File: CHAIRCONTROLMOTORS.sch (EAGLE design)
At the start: 39 parts, among them IC2 TCAN332DR, IC3 ATMEGA328P, IC4 MCP2515

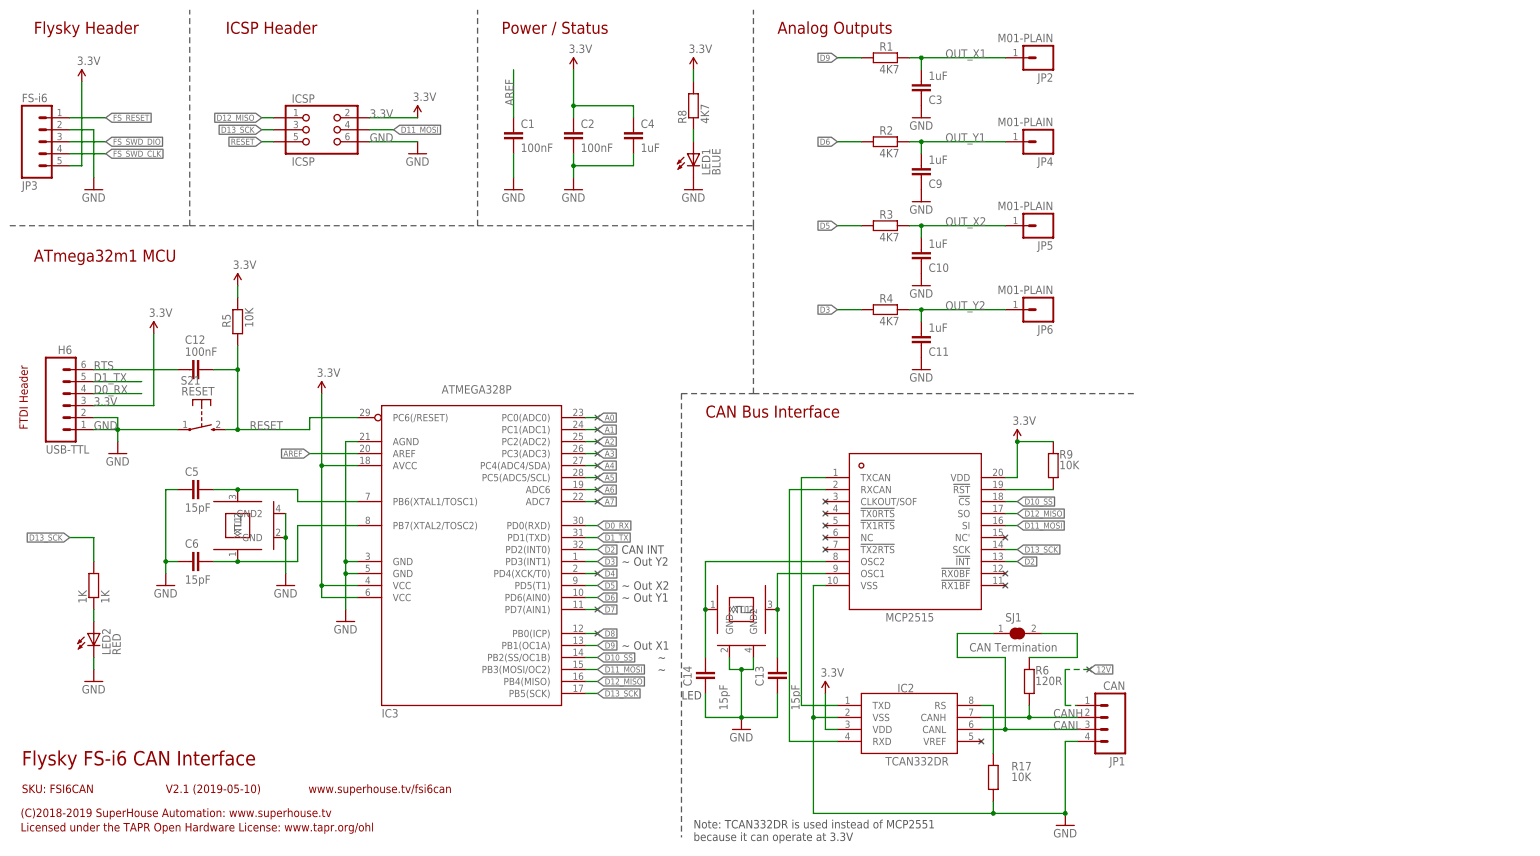
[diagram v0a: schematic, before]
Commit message: Added XTxx external connections
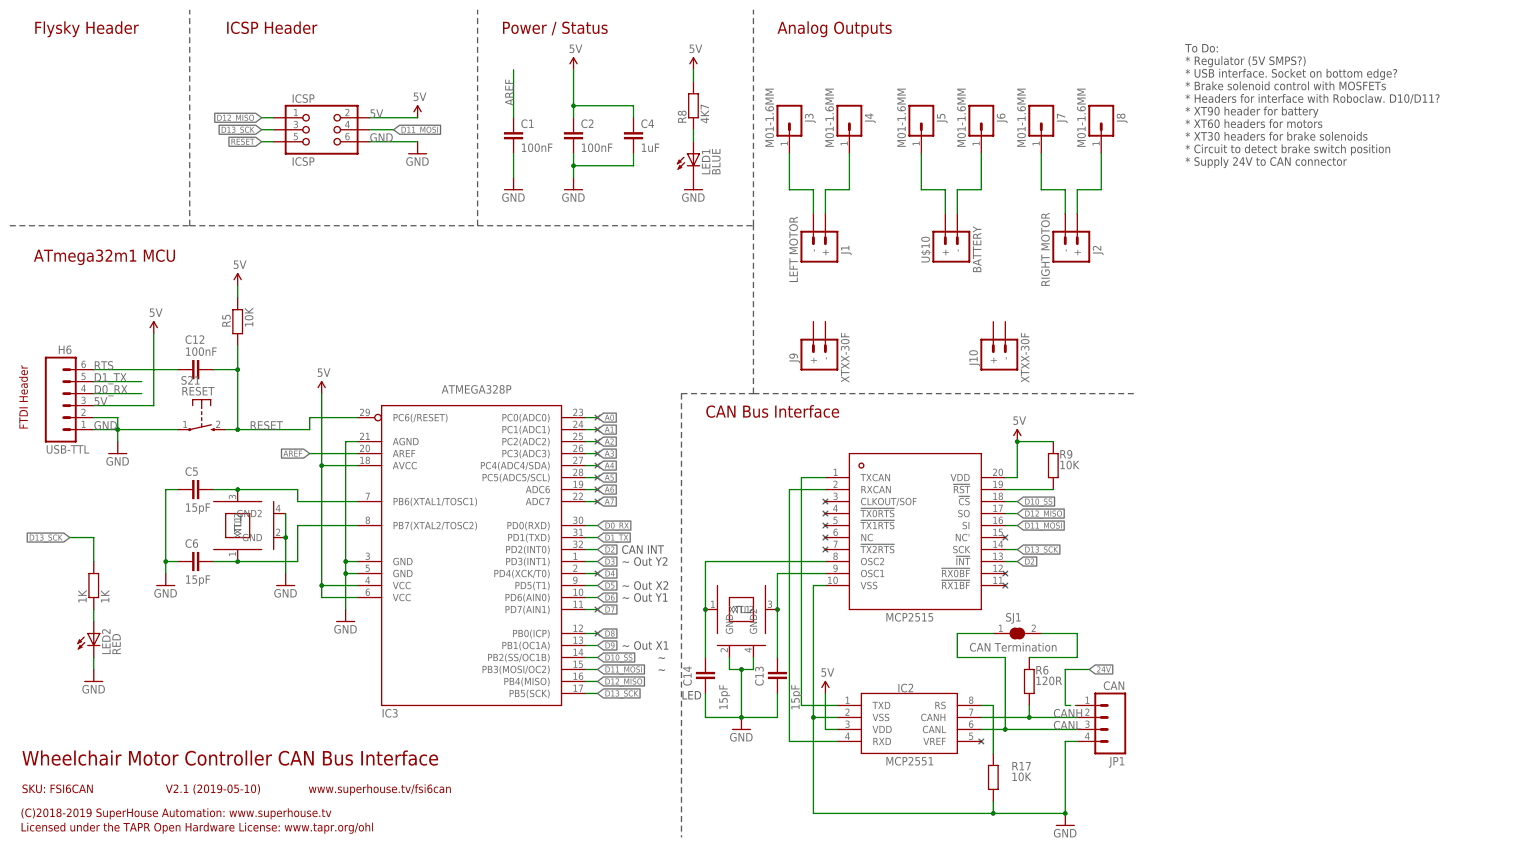
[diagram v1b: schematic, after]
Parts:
- removed C10, C11, C3, C9: 1uF, SuperHouse-DiscreteSemi:CAP0603
- removed JP2, JP4, JP5, JP6: M01-PLAIN, SuperHouse-Connectors:M01-PLAIN
- removed JP3: FS-i6, freetronics-jon:M05PTH
- removed R1, R2, R3, R4: 4K7, SuperHouse-DiscreteSemi:RESISTOR0603
- added J1: LEFT MOTOR, SuperHouse-Connectors:XTXX-60F
- added J10, J9: XTXX-30F, SuperHouse-Connectors:XTXX-30F
- added J2: RIGHT MOTOR, SuperHouse-Connectors:XTXX-60F
- added J3, J4, J5, J6, J7, J8: M01-1.6MM, SuperHouse-Connectors:M01-1.6MM
- added U$10: BATTERY, SuperHouse-Connectors:XTXX-90M
- IC2: value TCAN332DR -> MCP2551
- XTL1: value 8MHz -> 16MHz
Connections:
- net 12V renamed 24V
- removed net 3.3V: C2.1, C4.1, H6.3, IC2.VDD, IC3.AVCC, IC3.VCC@1, IC3.VCC@2, IC4.VDD, ICSP.2, JP3.5, R5.1, R8.2, R9.2
- removed net FS_RESET: JP3.1
- removed net FS_SWD_CLK: JP3.4
- removed net FS_SWD_DIO: JP3.3
- removed net OUT_X1: C3.1, JP2.1, R1.2
- removed net OUT_X2: C10.1, JP5.1, R3.2
- removed net OUT_Y1: C9.1, JP4.1, R2.2
- removed net OUT_Y2: C11.1, JP6.1, R4.2
- new net 5V: C2.1, C4.1, H6.3, IC2.VDD, IC3.AVCC, IC3.VCC@1, IC3.VCC@2, IC4.VDD, ICSP.2, R5.1, R8.2, R9.2
- new net N$10: J5.1, U$10.+
- new net N$13: J6.1, U$10.-
- new net N$14: J2.-, J7.1
- new net N$15: J2.+, J8.1
- new net N$3: J1.+, J4.1
- new net N$9: J1.-, J3.1
- net D3: no longer R4.1
- net D5: no longer R3.1
- net D6: no longer R2.1
- net D9: no longer R1.1
- net GND: no longer C10.2, C11.2, C3.2, C9.2, JP3.2
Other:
- note added: "To Do: * Regulator (5V SMPS?) * USB interface. Socket on bottom edge? * Brake solenoid control with MOSFETs * Headers for interface with Roboclaw. D10/D11? * XT90 header for battery * XT60 headers for motors * XT30 headers for brake solenoids * Circuit to detect brake switch position * Supply 24V to CAN connector"
- note added: "Wheelchair Motor Controller CAN Bus Interface"
- note removed: "Flysky FS-i6 CAN Interface"
- note removed: "Note: TCAN332DR is used instead of MCP2551 because it can operate at 3.3V"

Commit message: Major schematic replacement to switch to 32U4 processor
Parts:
- removed 1K: 1K, SuperHouse-DiscreteSemi:RESISTOR0603
- removed C1, C12, C2: 100nF, SuperHouse-DiscreteSemi:CAP0603
- removed C13, C14, C5, C6: 15pF, SuperHouse-DiscreteSemi:CAP0603
- removed C4: 1uF, SuperHouse-DiscreteSemi:CAP0603
- removed H6: USB-TTL, SuperHouse-Connectors:M06-PIN-RIGHTANGLE
- removed IC2: MCP2551, SuperHouse-ICs:MCP2551
- removed IC3: ATMEGA328P, SuperHouse-MCUs:ATMEGA8-AI
- removed IC4: MCP2515, SuperHouse-ICs:MCP2515
- removed ICSP: ICSP, SuperHouse-Connectors:ICSP-PIN
- removed JP1: CAN, SuperHouse-Connectors:M04-PIN
- removed LED1: BLUE, SuperHouse-LEDs:LED0603
- removed LED2: RED, SuperHouse-LEDs:LED0603
- removed R17, R5, R9: 10K, SuperHouse-DiscreteSemi:RESISTOR0603
- removed R6: 120R, SuperHouse-DiscreteSemi:RESISTOR0603
- removed R8: 4K7, SuperHouse-DiscreteSemi:RESISTOR0603
- removed S21: RESET, SuperHouse-Switches:TAC_SWITCH_2PINSMT
- removed SJ1: CAN Termination, SuperHouse-Jumpers:SJC-NORMAL
- removed XTL1, XTL3: 16MHz, SuperHouse-Oscillators:CRYSTAL-GND3X2
- added C10, C15, C16, C9: 15pF, freetronics-master-v1.1:CAP0603
- added C11, C7: 1uF, freetronics-master-v1.1:CAP0603
- added C3, C8: 100nF, freetronics-master-v1.1:CAP0603
- added D1: 1N4004, freetronics-jon:DIODESMB
- added F2: 500mA PTC 1812, rcl:L-EUL1812
- added IC5: MCP2551, freetronics-original:MCP2551
- added IC6: MCP2515, MCP2515:MCP2515
- added IC7: ATMEGA32U4NT, freetronics-jon:ATMEGA32U4NT
- added ICSP1: ICSP, pinhead:PINHD-2X3
- added J11: USB-B-PTH, SuperHouse-Connectors:USB-B-PTH
- added J12: M02X3-PIN, SuperHouse-Connectors:M02X3-PIN
- added JP2: CAN, freetronics-jon:M04PTH
- added JP3, JP5: PWR, freetronics-jon:M02PTH
- added JP4: PWR, freetronics-jon:M03PTH
- added LED5: RED, freetronics-jon:LED0603
- added LED6, LED8: GREEN, freetronics-jon:LED0603
- added LED7: BLUE, freetronics-jon:LED0603
- added R19, R25, R26: 10K, freetronics-master-v1.1:RESISTOR0603
- added R20: 4K7, freetronics-jon:RESISTOR0603
- added R21, R22, R33: 1K, freetronics-jon:RESISTOR0603
- added R23, R24: 22R, freetronics-jon:RESISTOR0603
- added R34: 120R, freetronics-master-v1.1:RESISTOR0603
- added REG1: K7805-500R3, freetronics-jon:K78XX-500R3
- added S1: RESET, freetronics-jon:TAC_SWITCH_2PINSMT
- added XTL2, XTL4: 16MHz, freetronics-jon:CRYSTAL-GND3X2
- added Z1, Z2: PGB1010603, freetronics-master-v1.1:RESISTOR0603
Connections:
- removed net A6: IC3.ADC6
- removed net A7: IC3.ADC7
- removed net D0_RX: H6.4, IC3.PD0(RXD)
- removed net D10_SS: IC3.PB2(SS/OC1B), IC4.!CS
- removed net D11_MOSI: IC3.PB3(MOSI/OC2), IC4.SI, ICSP.4
- removed net D12_MISO: IC3.PB4(MISO), IC4.SO, ICSP.1
- removed net D13_SCK: 1K.2, IC3.PB5(SCK), IC4.SCK, ICSP.3
- removed net D1_TX: H6.5, IC3.PD1(TXD)
- removed net D2: IC3.PD2(INT0), IC4.!INT
- removed net D3: IC3.PD3(INT1)
- removed net D4: IC3.PD4(XCK/T0)
- removed net D6: IC3.PD6(AIN0)
- removed net D7: IC3.PD7(AIN1)
- removed net D8: IC3.PB0(ICP)
- removed net D9: IC3.PB1(OC1A)
- removed net N$1: 1K.1, LED2.A
- removed net N$11: C5.2, IC3.PB6(XTAL1/TOSC1), XTL1.XTL2
- removed net N$12: C6.2, IC3.PB7(XTAL2/TOSC2), XTL1.XTL1
- removed net N$16: IC2.RS, R17.2
- removed net N$17: IC4.!RST, R9.1
- removed net N$4: IC2.TXD, IC4.TXCAN
- removed net N$6: IC2.RXD, IC4.RXCAN
- removed net N$7: C13.2, IC4.OSC1, XTL3.XTL2
- removed net N$8: C14.2, IC4.OSC2, XTL3.XTL1
- removed net RTS: C12.1, H6.6
- new net 3V3: C11.2, IC7.UCAP
- new net D+: J11.D+, R24.1, Z2.2
- new net D-: J11.D-, R23.1, Z1.2
- new net D0: IC7.PD2(INT2/RXD1)
- new net D1: IC7.PD3(INT3/TXD1)
- new net D10_A11: IC6.!CS, IC7.PB6(OC1B/!OC4B!/ADC13)
- new net D11: IC7.PB7(OC0A/OC1C/RTS)
- new net D12: IC7.PD6(T1/OC4D/ADC9)
- new net D13: IC7.PC7(ICP3/CLK0/OC4A), R33.1
- new net D2_SDA: IC6.!INT, IC7.PD1(INT1/SDA)
- new net D3_SCL: IC7.PD0(INT0/OC0B/SCL)
- new net D4_A6: IC7.PD4(ICP1/ADC8)
- new net D6_A8: IC7.PD7(OC4D/ADC10/T0)
- new net D7_AIN0: IC7.PE6
- new net D8_A9: IC7.PB4(ADC11)
- new net D9_A10: IC7.PB5(OC1A/!OC4B!/ADC12)
- new net HWB: IC7.PE2(HWB)
- new net MISO: IC6.SO, IC7.PB3(PDO/MISO), ICSP1.1
- new net MOSI: IC6.SI, IC7.PB2(PDI/MOSI), ICSP1.4
- new net N$28: C9.2, IC7.XTAL1, XTL2.XTL2
- new net N$29: C10.2, IC7.XTAL2, XTL2.XTL1
- new net N$30: LED7.A, R20.1
- new net N$31: LED5.A, R21.1
- new net N$32: LED6.A, R22.1
- new net N$33: IC6.!RST, R25.1
- new net N$34: IC5.TXD, IC6.TXCAN
- new net N$35: IC5.RXD, IC6.RXCAN
- new net N$36: IC5.RS, R26.2
- new net N$37: C15.2, IC6.OSC2, XTL4.XTL2
- new net N$38: C16.2, IC6.OSC1, XTL4.XTL1
- new net N$39: JP2.1, JP3.2
- new net N$40: D1.C, F2.1
- new net N$43: LED8.A, R33.2
- new net N$44: JP5.2, R34.2
- new net RD+: IC7.D+, R24.2
- new net RD-: IC7.D-, R23.2
- new net RXLED_SS: IC7.PB0(SS), LED6.C
- new net SCK: IC6.SCK, IC7.PB1(SCK), ICSP1.3
- new net TX_LED: IC7.PD5(XCK/CTS), LED5.C
- new net USB+: D1.A, J11.VBUS
- net 24V: now also JP3.1, JP4.2, REG1.IN; no longer JP1.1
- net 5V: now also C3.1, C7.1, F2.2, IC5.VDD, IC6.VDD, IC7.AVCC, IC7.AVCC1, IC7.UVCC, IC7.VBUS, IC7.VCC, IC7.VCC1, ICSP1.2, R19.2, R20.2, R21.2, R22.2, R25.2, REG1.OUT; no longer C2.1, C4.1, H6.3, IC2.VDD, IC3.AVCC, IC3.VCC@1, IC3.VCC@2, IC4.VDD, ICSP.2, R5.1, R8.2, R9.2
- net A0: now also IC7.PF7(ADC7(TDI); no longer IC3.PC0(ADC0)
- net A1: now also IC7.PF6(ADC6/TDO); no longer IC3.PC1(ADC1)
- net A2: now also IC7.PF5(ADC5/TMS); no longer IC3.PC2(ADC2)
- net A3: now also IC7.PF4(ADC4/TCK); no longer IC3.PC3(ADC3)
- net A4: now also IC7.PF1(ADC1); no longer IC3.PC4(ADC4/SDA)
- net A5: now also IC7.PF0(ADC0); no longer IC3.PC5(ADC5/SCL)
- net AREF: now also C8.1, IC7.AREF; no longer C1.1, IC3.AREF
- net CANH: now also IC5.CANH, JP2.2, JP5.1; no longer IC2.CANH, JP1.2, R6.1
- net CANL: now also IC5.CANL, JP2.3, R34.1; no longer IC2.CANL, JP1.3, SJ1.1
- net D5: now also IC7.PC6(OC3A/!OC4A!); no longer IC3.PD5(T1)
- net GND: now also C10.1, C11.1, C15.1, C16.1, C3.2, C7.2, C8.2, C9.1, IC5.VSS, IC6.VSS, IC7.GND, IC7.GND1, IC7.GND2, IC7.GND3, IC7.UGND, ICSP1.6, J10.+, J11.GND, J11.SHIELD, J9.+, JP2.4, JP4.1, LED7.C, LED8.C, R26.1, REG1.GND, S1.P, XTL2.GND, XTL2.GND2, XTL4.GND, XTL4.GND2, Z1.1, Z2.1; no longer C1.2, C13.1, C14.1, C2.2, C4.2, C5.1, C6.1, H6.1, H6.2, IC2.VSS, IC3.AGND, IC3.GND@1, IC3.GND@2, IC4.VSS, ICSP.6, JP1.4, LED1.C, LED2.C, R17.1, S21.P, XTL1.GND, XTL1.GND2, XTL3.GND, XTL3.GND2
- net N$2: now also J9.-; no longer R6.2, SJ1.2
- net N$5: now also J10.-; no longer LED1.A, R8.1
- net RESET: now also IC7./RESET, ICSP1.5, R19.1, S1.S; no longer C12.2, IC3.PC6(/RESET), ICSP.5, R5.2, S21.S
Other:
- note added: "ATmega32U4 MCU"
- note added: "RoboClaw Outputs"
- note added: "To Do: * Brake solenoid control with MOSFETs * Headers for interface with Roboclaw. D10/D11? * Circuit to detect brake switch position * Supply 24V to CAN connector * Headers for jumpers to RoboClaw * Sub-board to jumper to RoboClaw"
- note removed: "ATmega32m1 MCU"
- note removed: "Analog Outputs"
- note removed: "CAN INT"
- note removed: "FTDI Header"
- note removed: "Flysky Header"
- note removed: "LED"
- note removed: "To Do: * Regulator (5V SMPS?) * USB interface. Socket on bottom edge? * Brake solenoid control with MOSFETs * Headers for interface with Roboclaw. D10/D11? * XT90 header for battery * XT60 headers for motors * XT30 headers for brake solenoids * Circuit to detect brake switch position * Supply 24V to CAN connector"
- note removed: "~"
- note removed: "~ Out X1"
- note removed: "~ Out X2"
- note removed: "~ Out Y1"
- note removed: "~ Out Y2"
